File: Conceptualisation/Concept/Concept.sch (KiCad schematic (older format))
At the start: 0 parts

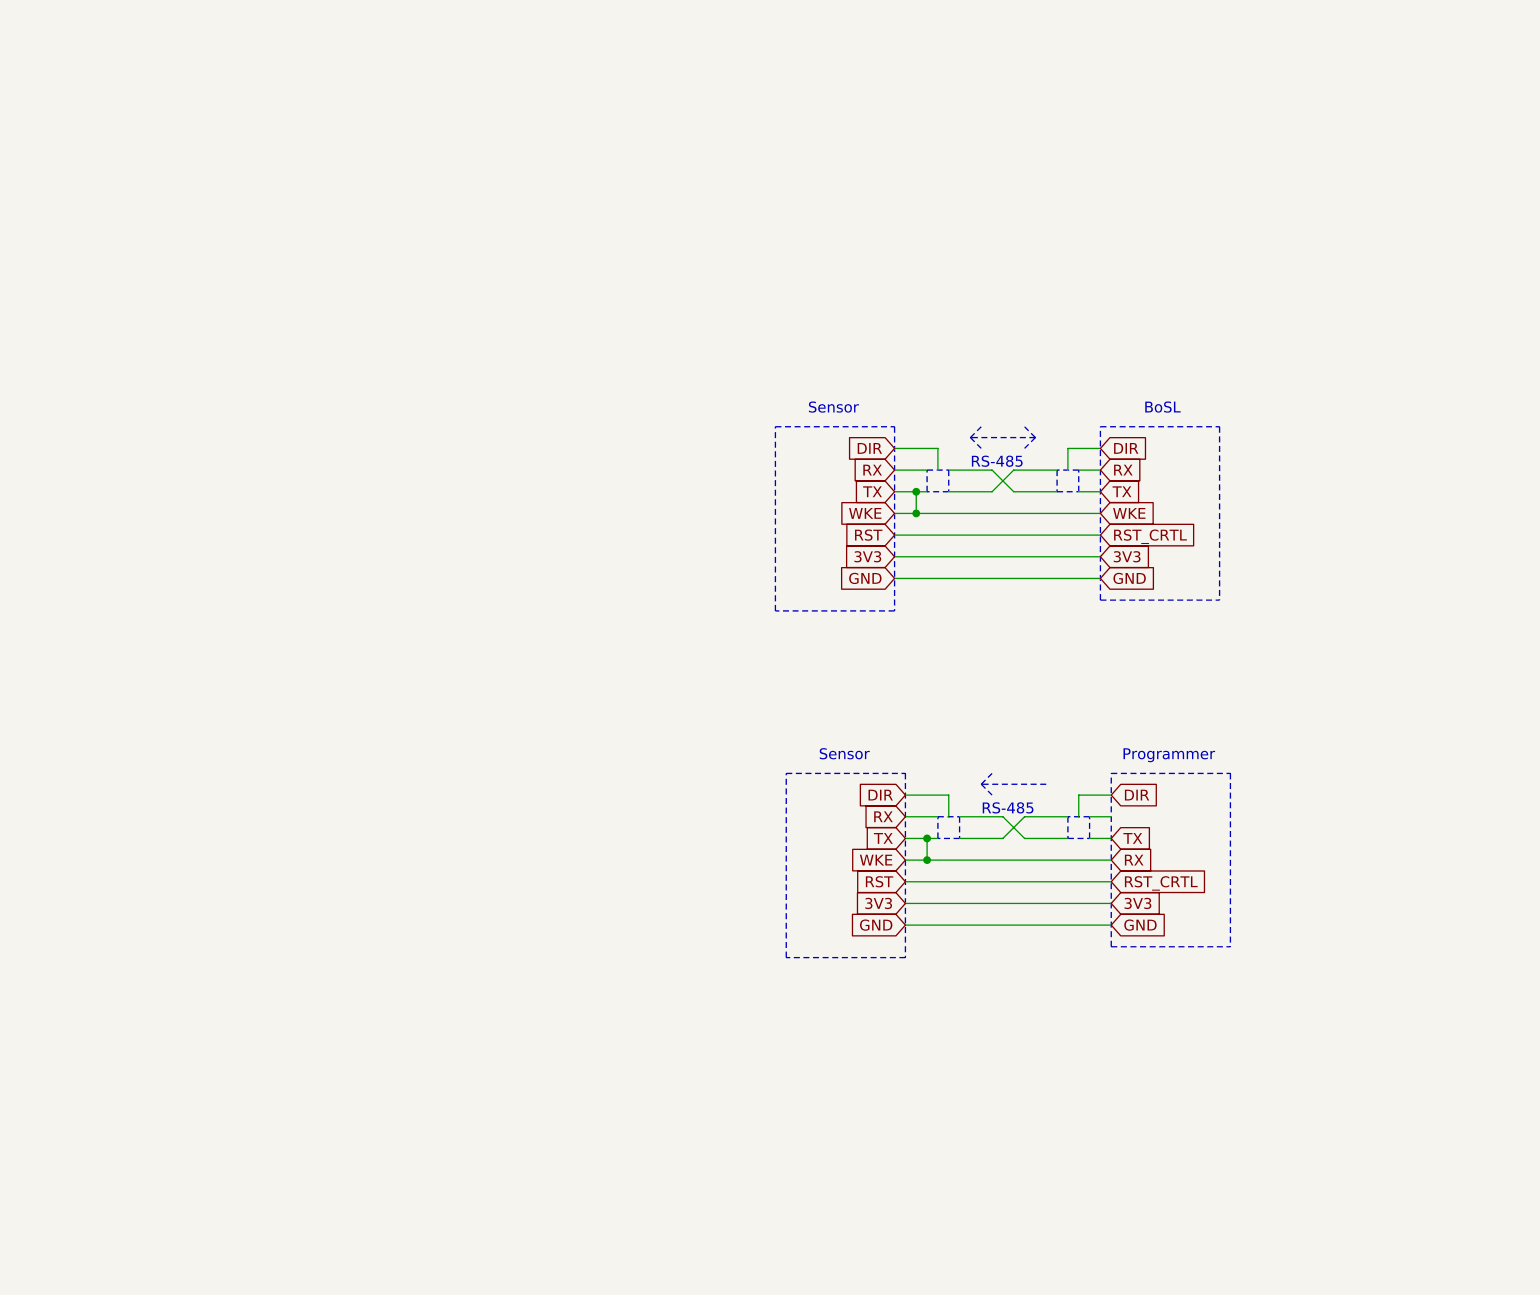
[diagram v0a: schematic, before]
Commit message: began ading implemtation of bosl_bus on atmega328p
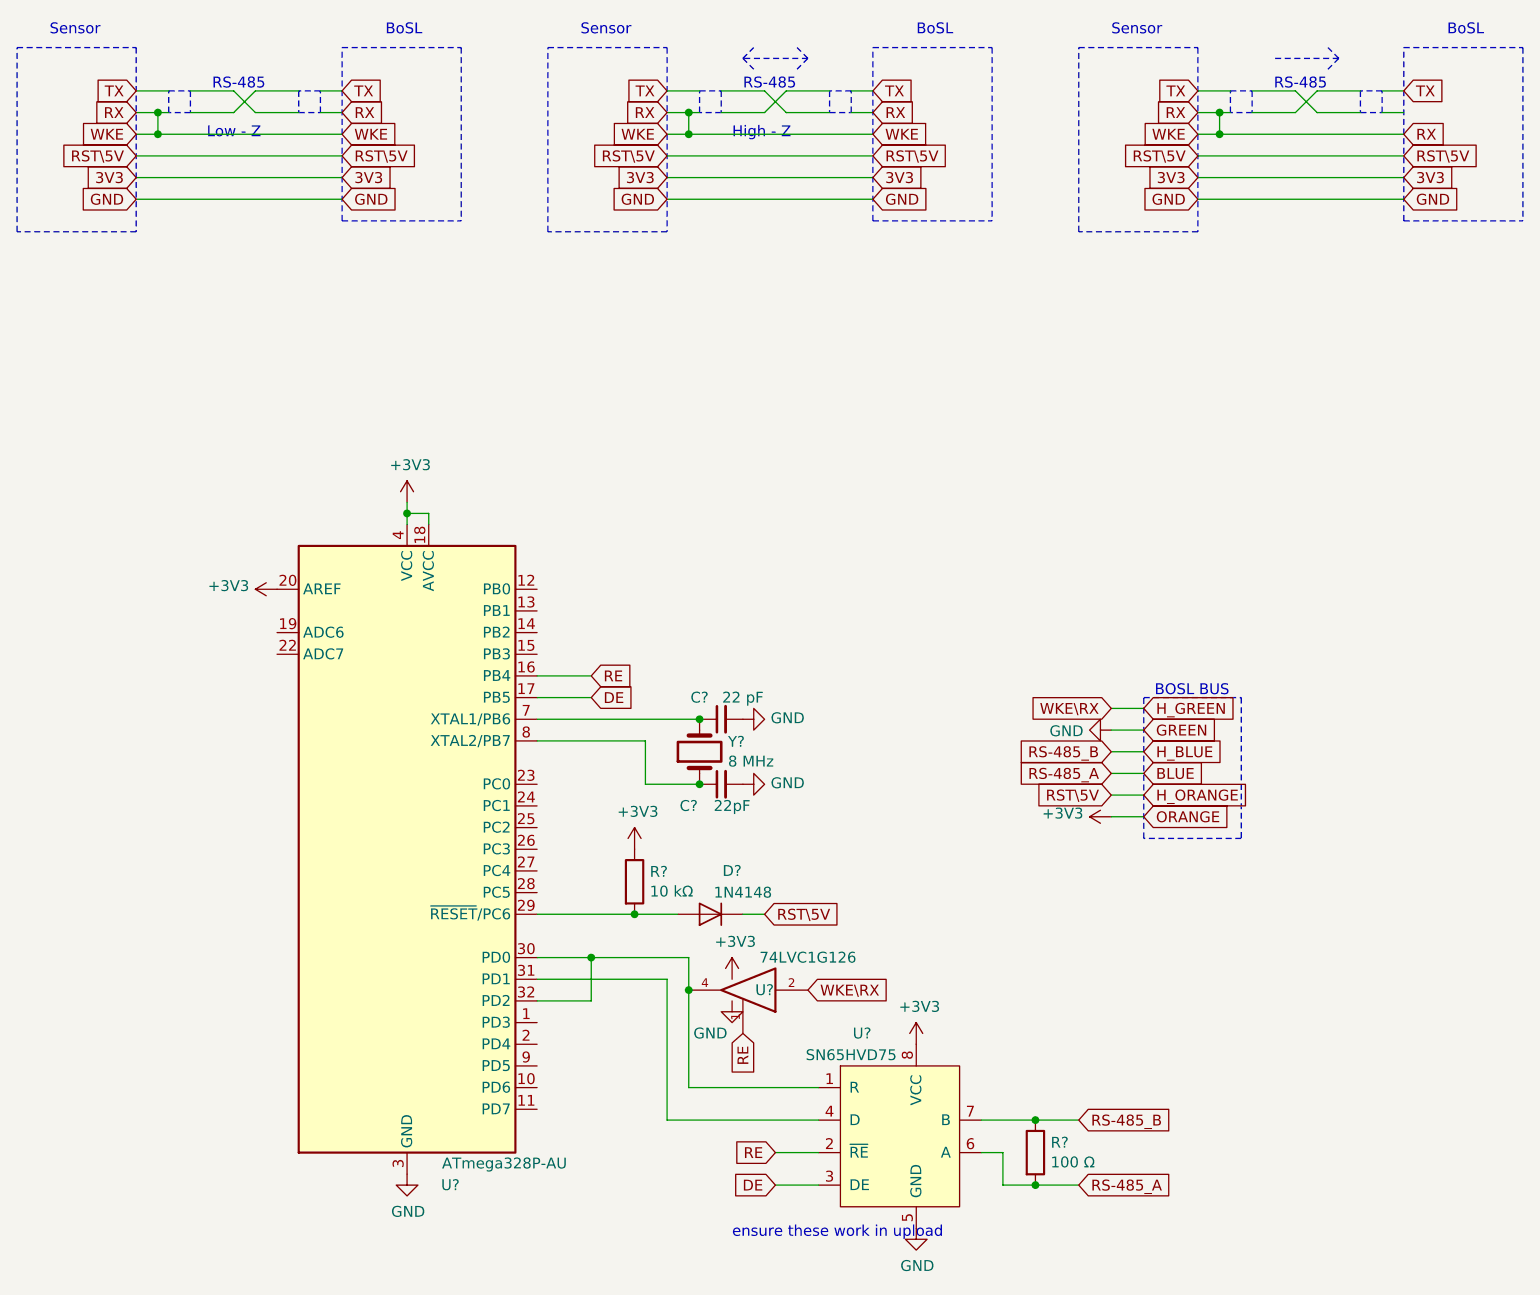
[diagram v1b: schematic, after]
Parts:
- added C?: 22 pF, symbol Device:C_Small
- added C?: 22pF, symbol Device:C_Small
- added D?: 1N4148, symbol Device:D
- added R?: 10 kΩ, symbol Device:R
- added R?: 100 Ω, symbol Device:R
- added U?: ATmega328P-AU, Package_QFP:TQFP-32_7x7mm_P0.8mm, symbol MCU_Microchip_ATmega:ATmega328P-AU
- added U?: SN65HVD75, symbol local:SN65HVD75
- added U?: 74LVC1G126, symbol 74xGxx:74LVC1G126
- added Y?: 8 MHz, symbol Device:Crystal
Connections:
- net labels added: +3V3, BLUE, DE, GREEN, H_BLUE, H_GREEN, H_ORANGE, ORANGE, RE, RS-485_A, RS-485_B, RST\5V, WKE\RX
- net labels removed: DIR, RST, RST_CRTL
- wire segments 42 -> 88
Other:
- note added: "BOSL BUS"
- note added: "High - Z"
- note added: "Low - Z"
- note added: "ensure these work in upload"
- note removed: "Programmer"

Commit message: daily commit
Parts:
- removed D?: 1N4148, symbol Device:D
- added D1: BAT54W, Package_TO_SOT_SMD:SOT-323_SC-70, symbol Diode:BAT54W
- added R1: 330 kΩ, symbol Device:R
- added R2: 47 kΩ, symbol Device:R
- gave numbers to parts that had none: 8
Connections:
- wire segments 88 -> 90
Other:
- note removed: "ensure these work in upload"

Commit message: added usart bosl bus schematic and pcb
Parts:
- R1: value 330 kΩ -> 1 MΩ
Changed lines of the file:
@@
 P 3300 5650
 F 0 "R1" H 3370 5696 50  0000 L CNN
-F 1 "330 kΩ" H 3370 5605 50  0000 L CNN
+F 1 "1 MΩ" H 3370 5605 50  0000 L CNN
 F 2 "" V 3230 5650 50  0001 C CNN
 F 3 "~" H 3300 5650 50  0001 C CNN
@@
 	3300 5500 3200 5500
 $Comp
-L power:GND #PWR04
-U 1 1 5F05F94F
-P 3300 5800
-F 0 "#PWR04" H 3300 5550 50  0001 C CNN
-F 1 "GND" H 3305 5627 50  0000 C CNN
-F 2 "" H 3300 5800 50  0001 C CNN
-F 3 "" H 3300 5800 50  0001 C CNN
-	1    3300 5800
-	1    0    0    -1
-$EndComp
-$Comp
 L Diode:BAT54W D1
 U 1 1 5F060523
@@
 	-1   0    0    1
 $EndComp
+$Comp
+L power:+3V3 #PWR?
+U 1 1 5F16F3C3
+P 3300 5800
+F 0 "#PWR?" H 3300 5650 50  0001 C CNN
+F 1 "+3V3" H 3315 5973 50  0000 C CNN
+F 2 "" H 3300 5800 50  0001 C CNN
+F 3 "" H 3300 5800 50  0001 C CNN
+	1    3300 5800
+	-1   0    0    1
+$EndComp
